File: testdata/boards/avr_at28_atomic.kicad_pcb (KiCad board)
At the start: 3 parts, among them U1 ATmega328P, U2 AT28C256

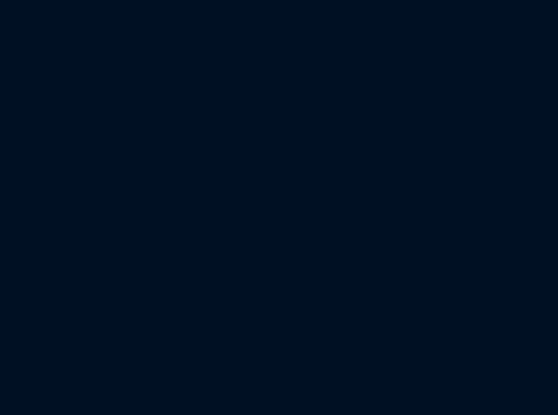
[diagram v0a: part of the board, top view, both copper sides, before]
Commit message: Guessed AVR clocks ride the verdict as their own conditions; fixture boards state their 16 MHz crystal
A guessed core clock is carried as a CiResult verdict condition (not mislabelled
as a partial member sweep). The demo and AT28 fixtures run firmware built for
16 MHz on a bare ATmega328P, so their boards now carry the 16 MHz crystal across
XTAL1/XTAL2 instead of relying on a hard-coded default. Classify backend_id.rs
in the doc-coverage inventory.

Signed-off-by: ETM-Code <158038827+ETM-Code@users.noreply.github.com>
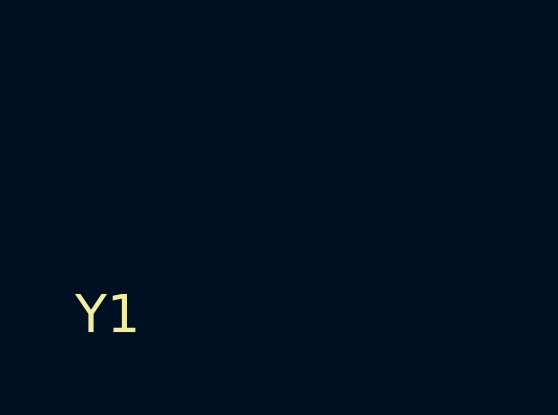
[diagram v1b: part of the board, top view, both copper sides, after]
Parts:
- added Y1: 16MHz, Crystal:Crystal_HC49-4H_Vertical, F.Cu at (100.0, 135.0)
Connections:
- U1 pad 10: GND -> XTAL2
- U1 pad 9: GND -> XTAL1
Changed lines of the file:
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@@
   (net 13 "OE_N")
   (net 14 "PASS")
+  (net 15 "XTAL1")
+  (net 16 "XTAL2")
   (module Package_DIP:DIP-28_W7.62mm (layer F.Cu)
     (at 100 100)
@@
     (pad 7 thru_hole circle (at 0 7) (size 1 1) (net 2 "+5V"))
     (pad 8 thru_hole circle (at 0 8) (size 1 1) (net 1 "GND"))
-    (pad 9 thru_hole circle (at 0 9) (size 1 1) (net 1 "GND"))
-    (pad 10 thru_hole circle (at 0 10) (size 1 1) (net 1 "GND"))
+    (pad 9 thru_hole circle (at 0 9) (size 1 1) (net 15 "XTAL1"))
+    (pad 10 thru_hole circle (at 0 10) (size 1 1) (net 16 "XTAL2"))
     (pad 11 thru_hole circle (at 0 11) (size 1 1) (net 1 "GND"))
     (pad 12 thru_hole circle (at 0 12) (size 1 1) (net 1 "GND"))
@@
     (pad 28 thru_hole circle (at 0 28) (size 1 1) (net 2 "+5V"))
   )
+  (module Crystal:Crystal_HC49-4H_Vertical (layer F.Cu)
+    (at 100 135)
+    (fp_text reference Y1 (at 0 0) (layer F.SilkS))
+    (fp_text value 16MHz (at 0 2) (layer F.Fab))
+    (pad 1 thru_hole circle (at 0 0) (size 1 1) (net 15 "XTAL1"))
+    (pad 2 thru_hole circle (at 4.9 0) (size 1 1) (net 16 "XTAL2"))
+  )
   (module Resistor:R (layer F.Cu)
